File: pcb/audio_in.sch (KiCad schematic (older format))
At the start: 15 parts, among them U7 MCP6409

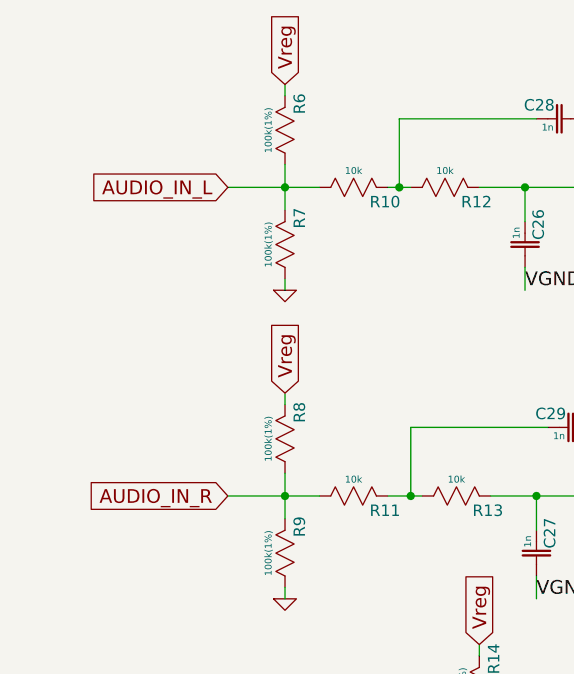
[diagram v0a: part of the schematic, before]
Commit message: Added DC blocking capacitors for audio in
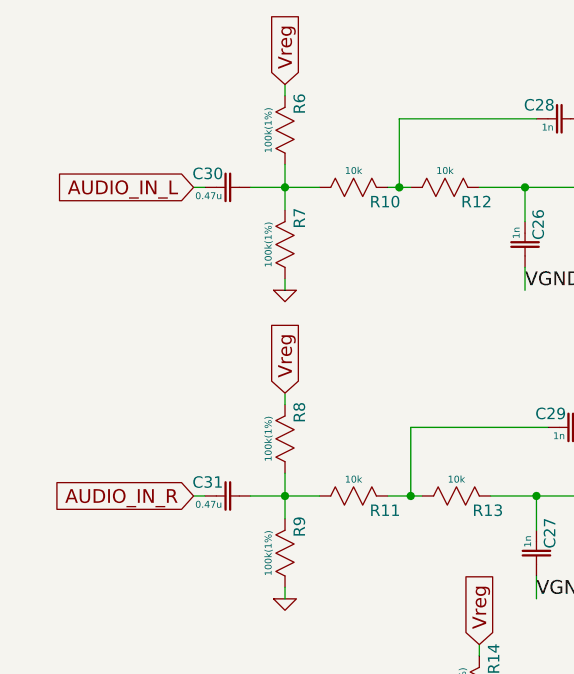
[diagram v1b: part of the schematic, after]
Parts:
- added C30, C31: 0.47u, symbol CAP
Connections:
- wire segments 44 -> 46
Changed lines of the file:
@@
-EESchema Schematic File Version 2  date Thu 26 Jul 2012 01:52:34 AM EDT
+EESchema Schematic File Version 2  date Thu 26 Jul 2012 02:06:26 AM EDT
 LIBS:power
 LIBS:device
@@
 	2050 2550 2050 2750
 Wire Wire Line
-	1800 2650 2200 2650
+	1900 2650 2200 2650
 Connection ~ 2050 2650
 Text GLabel 2050 2200 1    60   Input ~ 0
@@
 $EndComp
 Wire Wire Line
-	1800 4000 2200 4000
-Text GLabel 1800 2650 0    60   Input ~ 0
+	1900 4000 2200 4000
+Text GLabel 1650 2650 0    60   Input ~ 0
 AUDIO_IN_L
-Text GLabel 1800 4000 0    60   Input ~ 0
+Text GLabel 1650 4000 0    60   Input ~ 0
 AUDIO_IN_R
 Text GLabel 4350 4100 2    60   Input ~ 0
@@
 Text GLabel 4350 2750 2    60   Input ~ 0
 AUDIO_IN_PRE_R
+$Comp
+L CAP C30
+U 1 1 5010E008
+P 1800 2650
+F 0 "C30" H 1820 2620 50  0000 L TNN
+F 1 "0.47u" H 1825 2670 30  0000 L BNN
+	1    1800 2650
+	-1   0    0    1
+$EndComp
+$Comp
+L CAP C31
+U 1 1 5010E015
+P 1800 4000
+F 0 "C31" H 1820 3970 50  0000 L TNN
+F 1 "0.47u" H 1825 4020 30  0000 L BNN
+	1    1800 4000
+	-1   0    0    1
+$EndComp
+Wire Wire Line
+	1650 2650 1700 2650
+Wire Wire Line
+	1700 4000 1650 4000
 $EndSCHEMATC

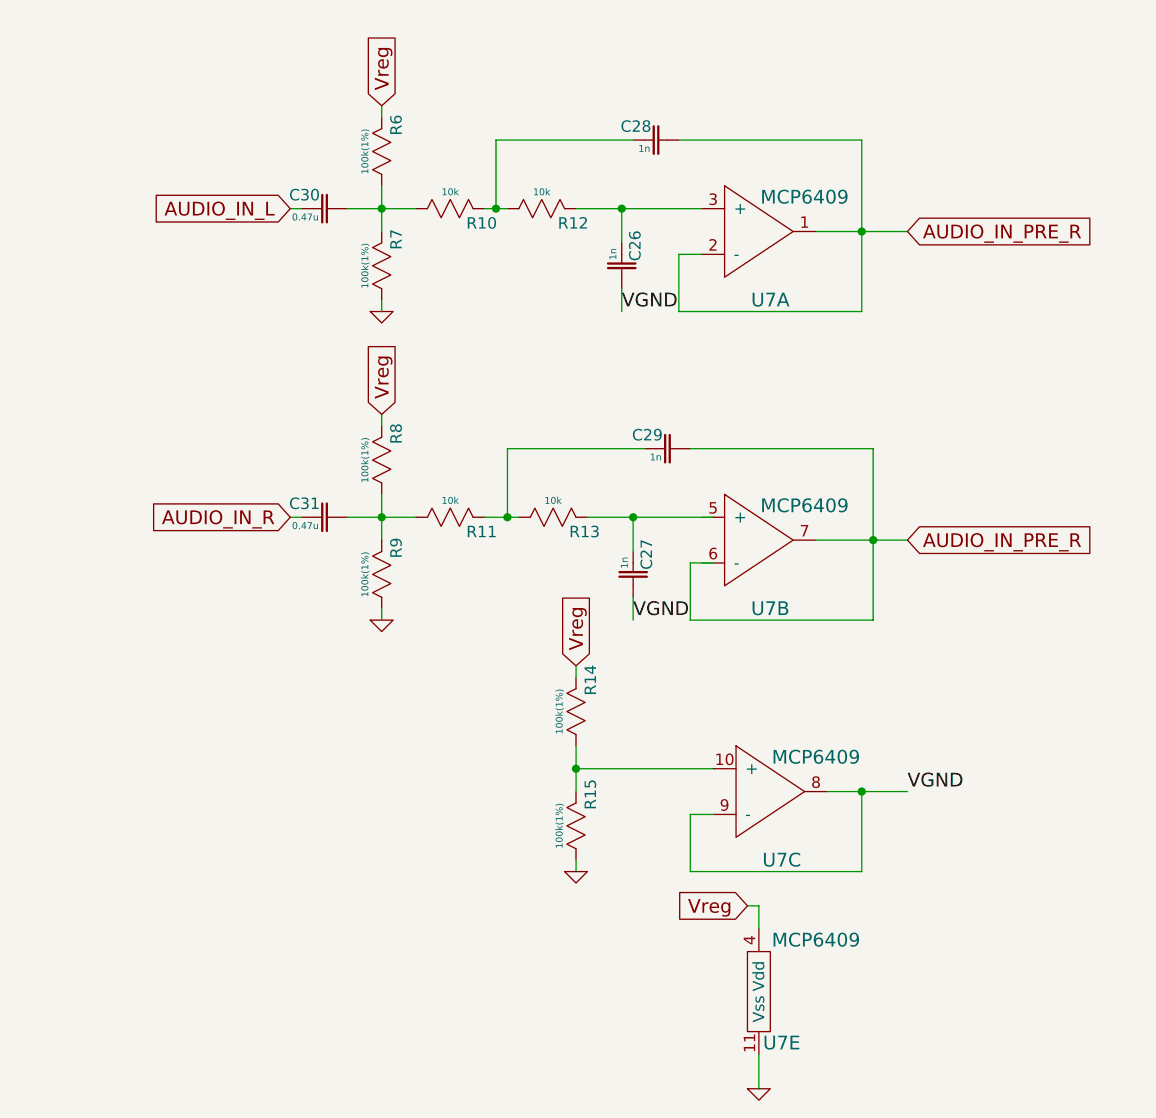
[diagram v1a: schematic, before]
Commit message: Changed filter values for 17kHz cutoff
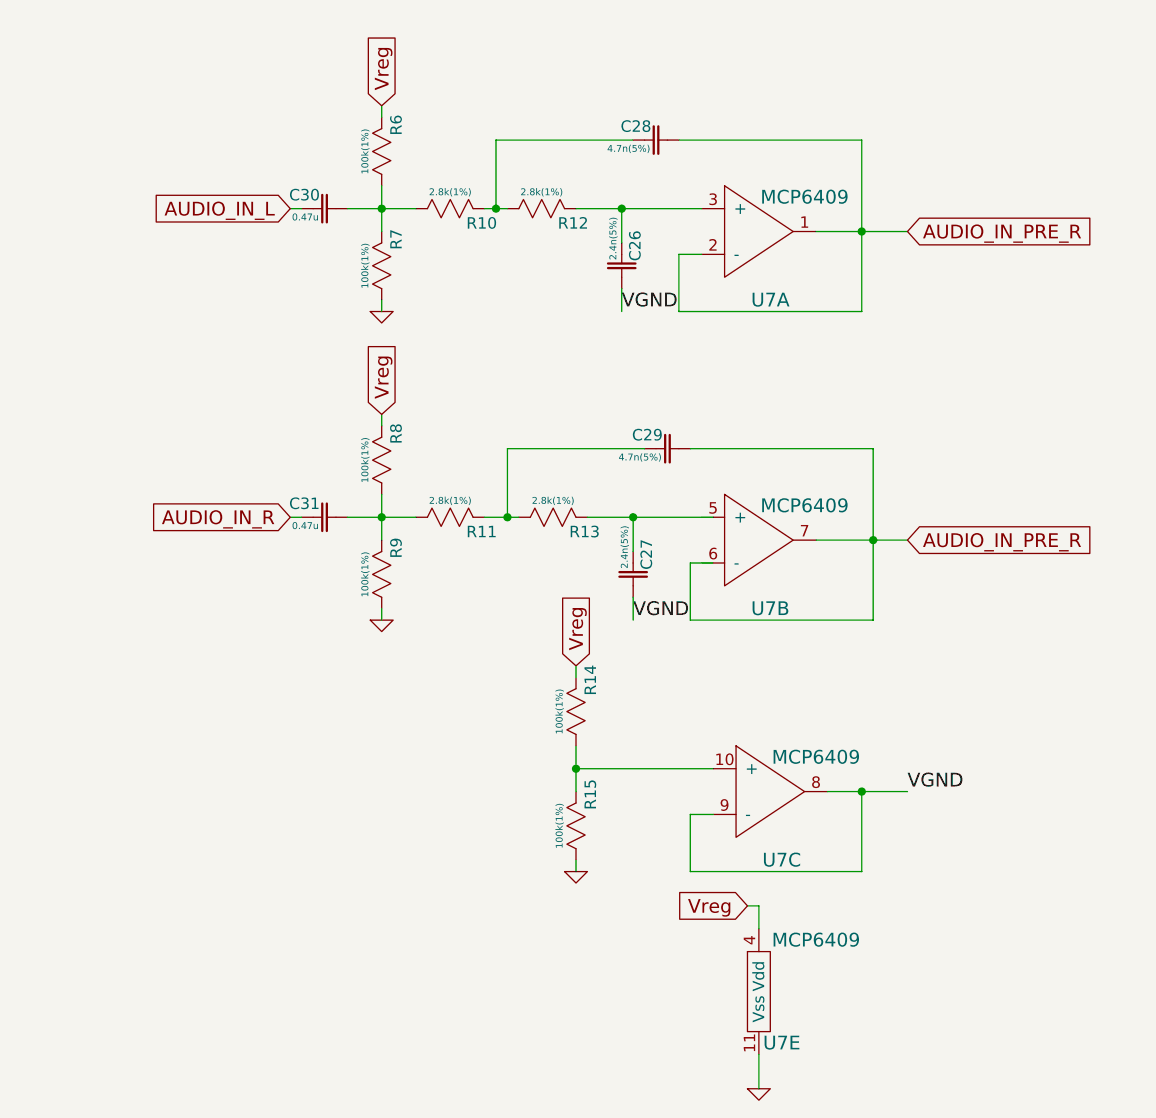
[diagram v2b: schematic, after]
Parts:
- C26, C27: value 1n -> 2.4n(5%)
- C28, C29: value 1n -> 4.7n(5%)
- R10, R11, R12, R13: value 10k -> 2.8k(1%)
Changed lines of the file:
@@
-EESchema Schematic File Version 2  date Thu 26 Jul 2012 02:06:26 AM EDT
+EESchema Schematic File Version 2  date Thu 26 Jul 2012 11:55:43 AM EDT
 LIBS:power
 LIBS:device
@@
 EELAYER 25  0
 EELAYER END
-$Descr A4 11693 8268
+$Descr A4 11700 8267
 encoding utf-8
 Sheet 5 5
@@
 P 2350 2650
 F 0 "R10" H 2420 2615 50  0000 L TNN
-F 1 "10k" H 2350 2705 30  0000 C BNN
+F 1 "2.8k(1%)" H 2350 2705 30  0000 C BNN
 	1    2350 2650
 	1    0    0    -1
@@
 P 2750 2650
 F 0 "R12" H 2820 2615 50  0000 L TNN
-F 1 "10k" H 2750 2705 30  0000 C BNN
+F 1 "2.8k(1%)" H 2750 2705 30  0000 C BNN
 	1    2750 2650
 	1    0    0    -1
@@
 P 3100 2900
 F 0 "C26" H 3120 2870 50  0000 L TNN
-F 1 "1n" H 3125 2920 30  0000 L BNN
+F 1 "2.4n(5%)" H 3125 2920 30  0000 L BNN
 	1    3100 2900
 	0    -1   -1   0
@@
 P 3250 2350
 F 0 "C28" H 3270 2320 50  0000 L TNN
-F 1 "1n" H 3275 2370 30  0000 L BNN
+F 1 "4.7n(5%)" H 3275 2370 30  0000 L BNN
 	1    3250 2350
 	-1   0    0    1
@@
 P 2800 4000
 F 0 "R13" H 2870 3965 50  0000 L TNN
-F 1 "10k" H 2800 4055 30  0000 C BNN
+F 1 "2.8k(1%)" H 2800 4055 30  0000 C BNN
 	1    2800 4000
 	1    0    0    -1
@@
 P 3150 4250
 F 0 "C27" H 3170 4220 50  0000 L TNN
-F 1 "1n" H 3175 4270 30  0000 L BNN
+F 1 "2.4n(5%)" H 3175 4270 30  0000 L BNN
 	1    3150 4250
 	0    -1   -1   0
@@
 P 3300 3700
 F 0 "C29" H 3320 3670 50  0000 L TNN
-F 1 "1n" H 3325 3720 30  0000 L BNN
+F 1 "4.7n(5%)" H 3325 3720 30  0000 L BNN
 	1    3300 3700
 	-1   0    0    1
@@
 P 2350 4000
 F 0 "R11" H 2420 3965 50  0000 L TNN
-F 1 "10k" H 2350 4055 30  0000 C BNN
+F 1 "2.8k(1%)" H 2350 4055 30  0000 C BNN
 	1    2350 4000
 	1    0    0    -1

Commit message: Added bypass cap for power on audio preamp
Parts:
- added C?: 100n, symbol CAP
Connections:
- wire segments 46 -> 49
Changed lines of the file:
@@
-EESchema Schematic File Version 2  date Thu 26 Jul 2012 11:55:43 AM EDT
+EESchema Schematic File Version 2  date Thu 26 Jul 2012 02:13:26 PM EDT
 LIBS:power
 LIBS:device
@@
 Comment4 ""
 $EndDescr
+Wire Wire Line
+	3700 5700 3950 5700
+Wire Wire Line
+	3700 5700 3700 5800
+Wire Wire Line
+	3700 6500 3700 6350
+Wire Wire Line
+	2050 2550 2050 2750
+Wire Wire Line
+	1900 2650 2200 2650
+Connection ~ 2050 2650
+Wire Wire Line
+	2050 2200 2050 2250
+Wire Wire Line
+	2550 2650 2550 2350
+Wire Wire Line
+	2550 2350 3150 2350
+Wire Wire Line
+	3350 2350 4150 2350
+Wire Wire Line
+	4150 2350 4150 3100
+Wire Wire Line
+	3950 2750 4350 2750
+Wire Wire Line
+	2900 2650 3450 2650
+Wire Wire Line
+	3100 2650 3100 2800
+Connection ~ 3100 2650
+Wire Wire Line
+	2500 2650 2600 2650
+Connection ~ 2550 2650
+Wire Wire Line
+	2050 3100 2050 3050
+Wire Wire Line
+	3450 2850 3350 2850
+Wire Wire Line
+	3350 2850 3350 3100
+Wire Wire Line
+	3350 3100 4150 3100
+Connection ~ 4150 2750
+Wire Wire Line
+	2900 5000 2900 5200
+Wire Wire Line
+	2900 5100 3500 5100
+Connection ~ 2900 5100
+Wire Wire Line
+	2600 4000 2600 3700
+Wire Wire Line
+	2600 3700 3200 3700
+Wire Wire Line
+	3400 3700 4200 3700
+Wire Wire Line
+	2950 4000 3500 4000
+Wire Wire Line
+	3150 4000 3150 4150
+Connection ~ 3150 4000
+Wire Wire Line
+	2500 4000 2650 4000
+Connection ~ 2600 4000
+Wire Wire Line
+	2900 5550 2900 5500
+Wire Wire Line
+	3500 4200 3400 4200
+Wire Wire Line
+	3400 4200 3400 4450
+Wire Wire Line
+	3400 4450 4200 4450
+Wire Wire Line
+	4200 4450 4200 3700
+Wire Wire Line
+	3950 4100 4350 4100
+Connection ~ 4200 4100
+Wire Wire Line
+	2900 4650 2900 4700
+Wire Wire Line
+	3500 5300 3400 5300
+Wire Wire Line
+	3400 5300 3400 5550
+Wire Wire Line
+	3400 5550 4150 5550
+Wire Wire Line
+	4150 5550 4150 5200
+Wire Wire Line
+	4000 5200 4350 5200
+Connection ~ 4150 5200
+Wire Wire Line
+	3100 3100 3100 3000
+Wire Wire Line
+	3150 4350 3150 4450
+Wire Wire Line
+	2050 3900 2050 4100
+Connection ~ 2050 4000
+Wire Wire Line
+	2050 4450 2050 4400
+Wire Wire Line
+	2050 3550 2050 3600
+Wire Wire Line
+	1900 4000 2200 4000
+Wire Wire Line
+	1650 2650 1700 2650
+Wire Wire Line
+	1700 4000 1650 4000
+Wire Wire Line
+	3950 5700 3950 5950
+Connection ~ 3700 5700
+Wire Wire Line
+	3950 6150 3950 6400
+Connection ~ 3700 6400
+Wire Wire Line
+	3950 6400 3700 6400
+$Comp
+L CAP C?
+U 1 1 50118878
+P 3950 6050
+F 0 "C?" H 3970 6020 50  0000 L TNN
+F 1 "100n" H 3975 6070 30  0000 L BNN
+	1    3950 6050
+	0    -1   -1   0
+$EndComp
 $Comp
 L MCP6409 U7
@@
 P 3700 6000
 F 0 "U7" H 3800 5700 60  0000 C CNN
-F 1 "MCP6409" H 3950 6150 60  0000 C CNN
+F 1 "MCP6409" H 3400 6150 60  0000 C CNN
 	5    3700 6000
 	1    0    0    -1
@@
 Text GLabel 3650 5700 0    60   Input ~ 0
 Vreg
-Wire Wire Line
-	3650 5700 3700 5700
-Wire Wire Line
-	3700 5700 3700 5800
 $Comp
 L GND #PWR25
@@
 	1    0    0    -1
 $EndComp
-Wire Wire Line
-	3700 6500 3700 6350
 $Comp
 L RES R10
@@
 	-1   0    0    1
 $EndComp
-Wire Wire Line
-	2050 2550 2050 2750
-Wire Wire Line
-	1900 2650 2200 2650
-Connection ~ 2050 2650
 Text GLabel 2050 2200 1    60   Input ~ 0
 Vreg
-Wire Wire Line
-	2050 2200 2050 2250
-Wire Wire Line
-	2550 2650 2550 2350
-Wire Wire Line
-	2550 2350 3150 2350
-Wire Wire Line
-	3350 2350 4150 2350
-Wire Wire Line
-	4150 2350 4150 3100
-Wire Wire Line
-	3950 2750 4350 2750
-Wire Wire Line
-	2900 2650 3450 2650
-Wire Wire Line
-	3100 2650 3100 2800
-Connection ~ 3100 2650
-Wire Wire Line
-	2500 2650 2600 2650
-Connection ~ 2550 2650
 $Comp
 L GND #PWR22
@@
 	1    0    0    -1
 $EndComp
-Wire Wire Line
-	2050 3100 2050 3050
-Wire Wire Line
-	3450 2850 3350 2850
-Wire Wire Line
-	3350 2850 3350 3100
-Wire Wire Line
-	3350 3100 4150 3100
-Connection ~ 4150 2750
 $Comp
 L RES R13
@@
 	-1   0    0    1
 $EndComp
-Wire Wire Line
-	2900 5000 2900 5200
-Wire Wire Line
-	2900 5100 3500 5100
-Connection ~ 2900 5100
 Text GLabel 2900 4650 1    60   Input ~ 0
 Vreg
-Wire Wire Line
-	2600 4000 2600 3700
-Wire Wire Line
-	2600 3700 3200 3700
-Wire Wire Line
-	3400 3700 4200 3700
-Wire Wire Line
-	2950 4000 3500 4000
-Wire Wire Line
-	3150 4000 3150 4150
-Connection ~ 3150 4000
-Wire Wire Line
-	2500 4000 2650 4000
-Connection ~ 2600 4000
 $Comp
 L GND #PWR24
@@
 	1    0    0    -1
 $EndComp
-Wire Wire Line
-	2900 5550 2900 5500
-Wire Wire Line
-	3500 4200 3400 4200
-Wire Wire Line
-	3400 4200 3400 4450
-Wire Wire Line
-	3400 4450 4200 4450
-Wire Wire Line
-	4200 4450 4200 3700
-Wire Wire Line
-	3950 4100 4350 4100
-Connection ~ 4200 4100
-Wire Wire Line
-	2900 4650 2900 4700
-Wire Wire Line
-	3500 5300 3400 5300
-Wire Wire Line
-	3400 5300 3400 5550
-Wire Wire Line
-	3400 5550 4150 5550
-Wire Wire Line
-	4150 5550 4150 5200
-Wire Wire Line
-	4000 5200 4350 5200
-Connection ~ 4150 5200
 Text Label 4350 5200 0    60   ~ 0
 VGND
@@
 Text Label 3100 3100 0    60   ~ 0
 VGND
-Wire Wire Line
-	3100 3100 3100 3000
-Wire Wire Line
-	3150 4350 3150 4450
 $Comp
 L RES R8
@@
 	0    -1   -1   0
 $EndComp
-Wire Wire Line
-	2050 3900 2050 4100
-Connection ~ 2050 4000
 Text GLabel 2050 3550 1    60   Input ~ 0
 Vreg
@@
 	1    0    0    -1
 $EndComp
-Wire Wire Line
-	2050 4450 2050 4400
-Wire Wire Line
-	2050 3550 2050 3600
 $Comp
 L RES R11
@@
 	1    0    0    -1
 $EndComp
-Wire Wire Line
-	1900 4000 2200 4000
 Text GLabel 1650 2650 0    60   Input ~ 0
 AUDIO_IN_L
@@
 	-1   0    0    1
 $EndComp
-Wire Wire Line
-	1650 2650 1700 2650
-Wire Wire Line
-	1700 4000 1650 4000
 $EndSCHEMATC
